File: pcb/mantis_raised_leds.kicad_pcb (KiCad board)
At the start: 2 copper layers, 131.5 x 107.5 mm, 57 parts

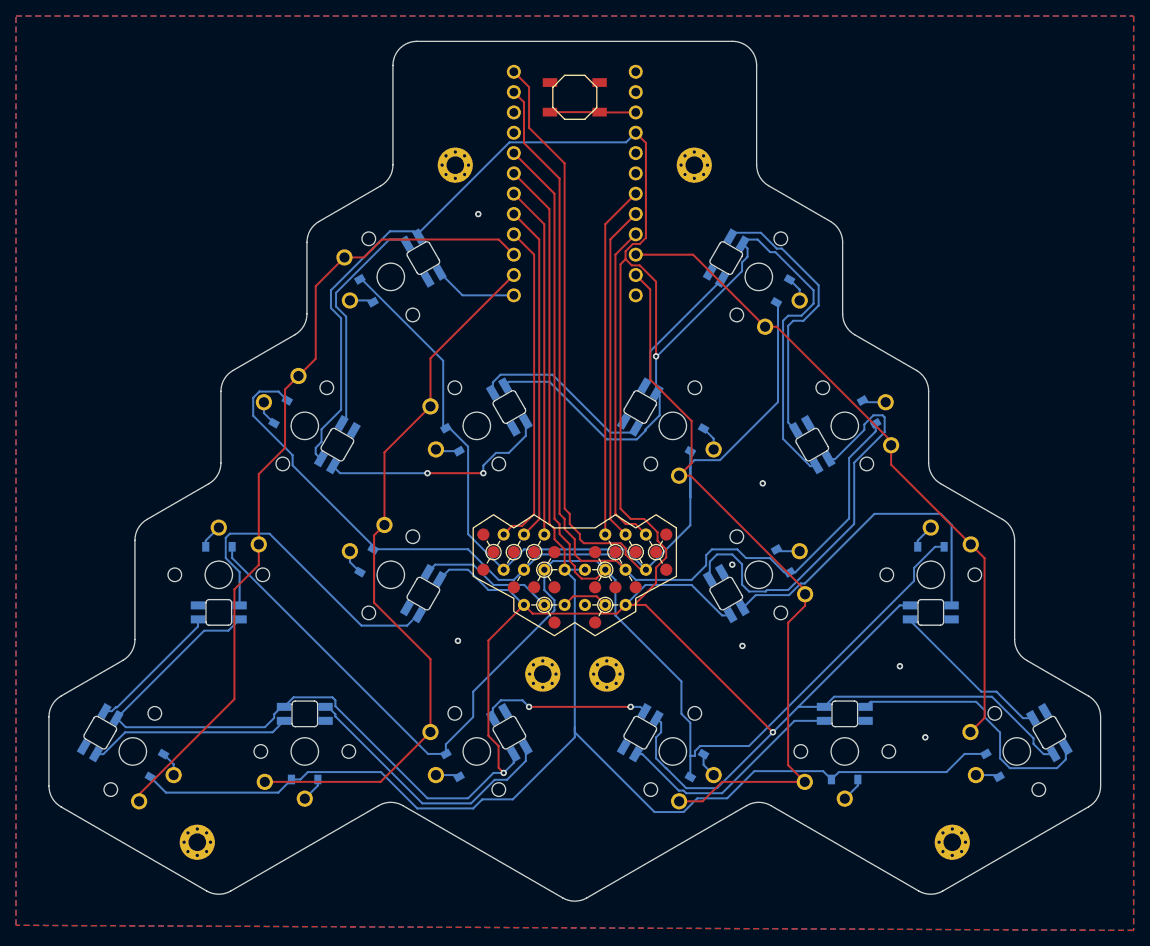
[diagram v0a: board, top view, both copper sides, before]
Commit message: pcb: Minor fixes and cleanups
Fix DRC warnings about silk screen intsecting edge cuts or solder mask.
Minor routing cleanups.

Signed-off-by: Felix Kuehling <felix.kuehling@gmail.com>
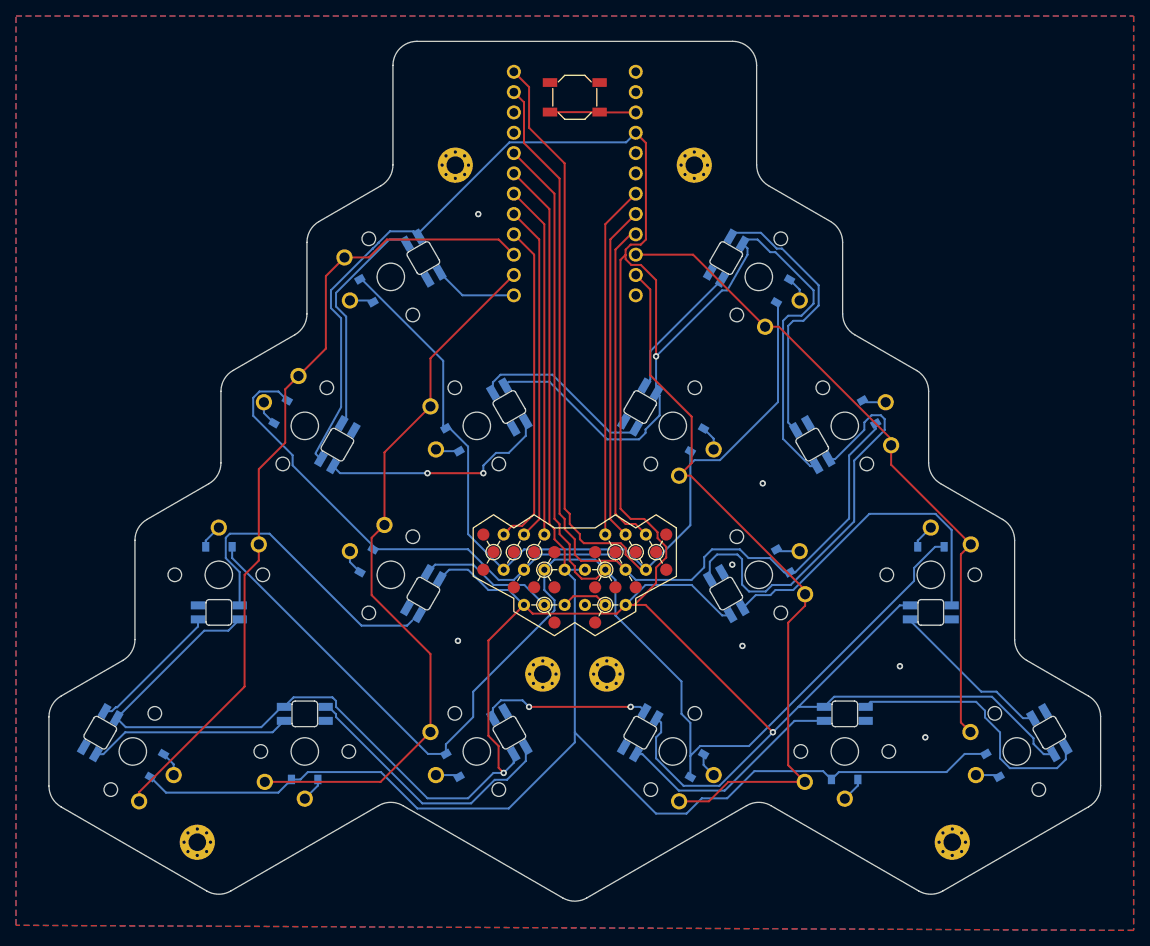
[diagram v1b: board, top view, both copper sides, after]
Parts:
- B1: footprint E73:SW_TACT_ALPS_SKQGABE010 -> Mantis:SW_TACT_ALPS_SKQGABE010
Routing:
- net R3: track 184.1 -> 180.0 mm
- net VCC: track 496.5 -> 495.4 mm

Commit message: pcb: Generated Gerber files for v0.3
Signed-off-by: Felix Kuehling <felix.kuehling@gmail.com>
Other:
- rule pad_to_mask_clearance: 0.05 -> 0
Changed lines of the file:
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@@
   )
   (setup
-    (pad_to_mask_clearance 0.05)
+    (stackup
+      (layer "F.SilkS" (type "Top Silk Screen"))
+      (layer "F.Paste" (type "Top Solder Paste"))
+      (layer "F.Mask" (type "Top Solder Mask") (thickness 0.01))
+      (layer "F.Cu" (type "copper") (thickness 0.035))
+      (layer "dielectric 1" (type "core") (thickness 1.51) (material "FR4") (epsilon_r 4.5) (loss_tangent 0.02))
+      (layer "B.Cu" (type "copper") (thickness 0.035))
+      (layer "B.Mask" (type "Bottom Solder Mask") (thickness 0.01))
+      (layer "B.Paste" (type "Bottom Solder Paste"))
+      (layer "B.SilkS" (type "Bottom Silk Screen"))
+      (copper_finish "None")
+      (dielectric_constraints no)
+    )
+    (pad_to_mask_clearance 0)
     (pcbplotparams
       (layerselection 0x00010fc_ffffffff)
@@
       (outputformat 1)
       (mirror false)
-      (drillshape 1)
+      (drillshape 0)
       (scaleselection 1)
       (outputdirectory "")

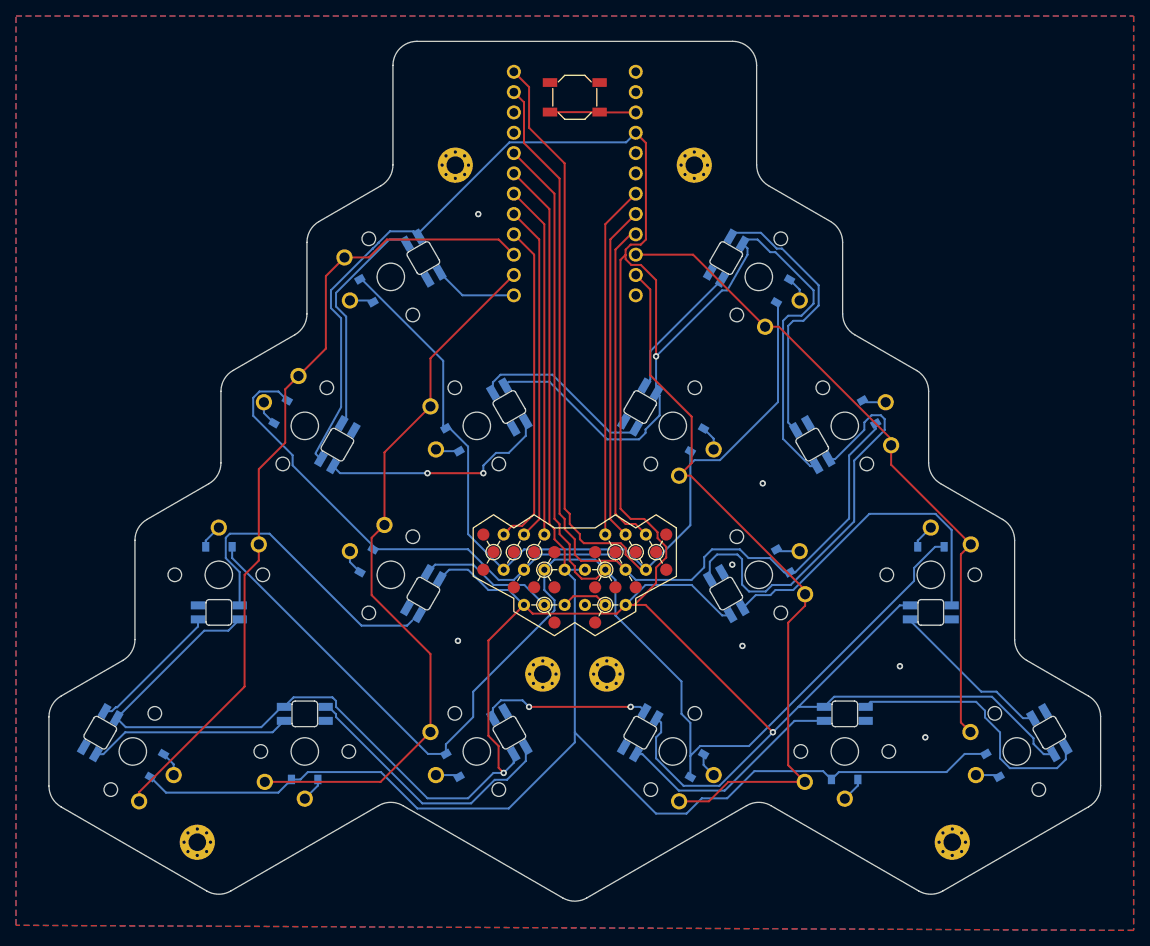
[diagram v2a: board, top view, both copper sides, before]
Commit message: pcb: Update raised PCB for v0.3.3
Changes since v0.3:
- Rotated inner bottom index finger keys
- Use RAW pin for LED power supply
- Added optional level shifter on LED data pin to support 3.3V controllers
  (Using two channels on a 6 channel inverter that's available on
  AdaFruit, cheap enough and simpler than building something from
  discrete resistor and transistor)
- Added jumper to bypass level shifter for 5V controllers
- Moved ProMicro pin labels on silkscreen to the outside to make room for
  level shifter
- Slightly increased silkscreen line widths on the mantis logo/headers
- Fixed unused pad number on header footprint
- Cleaned up some routing, removed two GND vias

Signed-off-by: Felix Kuehling <felix.kuehling@gmail.com>
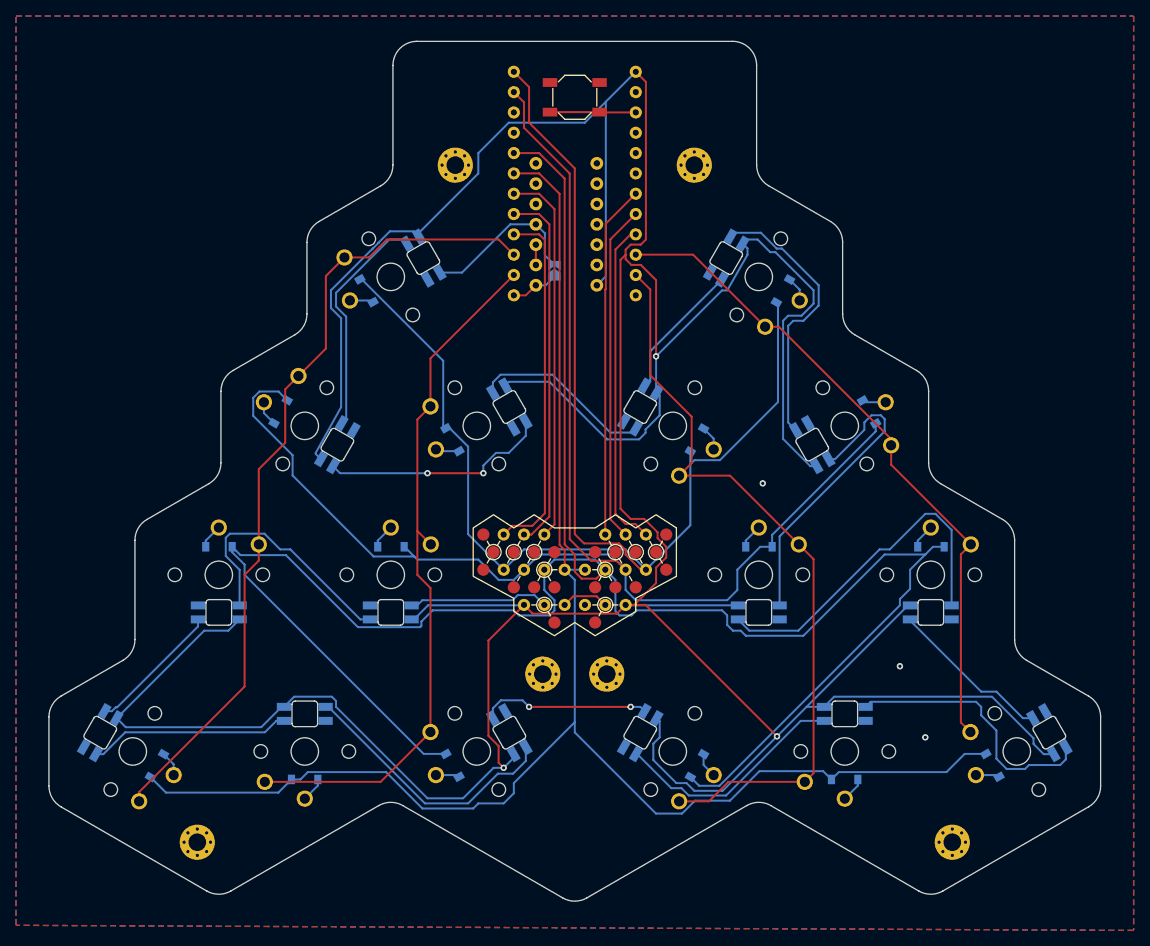
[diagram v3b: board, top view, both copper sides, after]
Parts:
- added Direct: SolderJumper-2_P1.3mm_Open_TrianglePad1.0x1.5mm, Jumper:SolderJumper-2_P1.3mm_Open_TrianglePad1.0x1.5mm, B.Cu at (251.5, 89.0)
- added LED level shifter: DIP-14_W7.62mm, Package_DIP:DIP-14_W7.62mm, B.Cu at (249.1, 90.8)
- B1: footprint Mantis:SW_TACT_ALPS_SKQGABE010 -> E73:SW_TACT_ALPS_SKQGABE010
- moved LED4 4.70 mm to (231.0, 131.7), turned to 180 degrees
- moved LED12 4.70 mm to (277.0, 131.7), turned to 0 degrees
- moved D12 3.50 mm to (277.0, 123.5), turned to 180 degrees
- moved D4 3.50 mm to (231.0, 123.5), turned to 180 degrees
- turned S12 to 0 degrees
- turned S4 to 0 degrees
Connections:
- MCU1 pad 1: RAW -> VCC
- MCU1 pad 24: di_c4_r3 -> LED
- MCU1 pad 4: VCC -> 3_3V
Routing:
- net R1: track 210.1 -> 258.5 mm
- net VCC: track 495.4 -> 532.0 mm
- net di_mirror_c5_r2: track 52.4 -> 38.7 mm
- net di_c4_r3: track 10.4 -> 20.5 mm
- net LED: track 0.00 -> 6.05 mm
- net di_c5_r2: track 37.7 -> 31.9 mm
- net C3: track 40.9 -> 44.6 mm
- net C2: track 42.2 -> 45.6 mm
- net C1: track 44.2 -> 47.1 mm
- net (no net): track 0.00 -> 2.54 mm
- net RT: track 196.6 -> 199.0 mm
- net C5: track 90.8 -> 88.5 mm
- net di_mirror_c4_r1: track 41.3 -> 43.6 mm
- net M_C5: track 92.7 -> 94.8 mm
- net do_c5_r2: track 17.0 -> 17.6 mm
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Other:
- outline, holes or cut-outs redrawn
- rule pad_to_mask_clearance: 0 -> 0.05
- board text added: "Mantis v0.3.3 Felix Kühling November 2023"
- board text removed: "Mantis v0.3 Felix Kühling July 2023"

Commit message: pcb: Top PCB v0.3.3 Gerbers
Signed-off-by: Felix Kuehling <felix.kuehling@gmail.com>
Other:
- rule pad_to_mask_clearance: 0.05 -> 0
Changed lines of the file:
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@@
   )
   (setup
-    (pad_to_mask_clearance 0.05)
+    (stackup
+      (layer "F.SilkS" (type "Top Silk Screen"))
+      (layer "F.Paste" (type "Top Solder Paste"))
+      (layer "F.Mask" (type "Top Solder Mask") (thickness 0.01))
+      (layer "F.Cu" (type "copper") (thickness 0.035))
+      (layer "dielectric 1" (type "core") (thickness 1.51) (material "FR4") (epsilon_r 4.5) (loss_tangent 0.02))
+      (layer "B.Cu" (type "copper") (thickness 0.035))
+      (layer "B.Mask" (type "Bottom Solder Mask") (thickness 0.01))
+      (layer "B.Paste" (type "Bottom Solder Paste"))
+      (layer "B.SilkS" (type "Bottom Silk Screen"))
+      (copper_finish "None")
+      (dielectric_constraints no)
+    )
+    (pad_to_mask_clearance 0)
     (pcbplotparams
       (layerselection 0x00010fc_ffffffff)
@@
       (outputformat 1)
       (mirror false)
-      (drillshape 1)
+      (drillshape 0)
       (scaleselection 1)
-      (outputdirectory "")
+      (outputdirectory "gerber/")
     )
   )
